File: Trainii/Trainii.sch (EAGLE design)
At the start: 30 parts, among them J1 APDS-9960, J2 Left Motor Encoder, J3 Right Motor Encoder, J4 Line Sensor 1, J5 Line Sensor 2, J6 Ultrasonic, J7 Left Motor Output, J8 Right Motor Output, J9 Lift Motor Output, U1 TPS61222DCKR, U2 BSS138

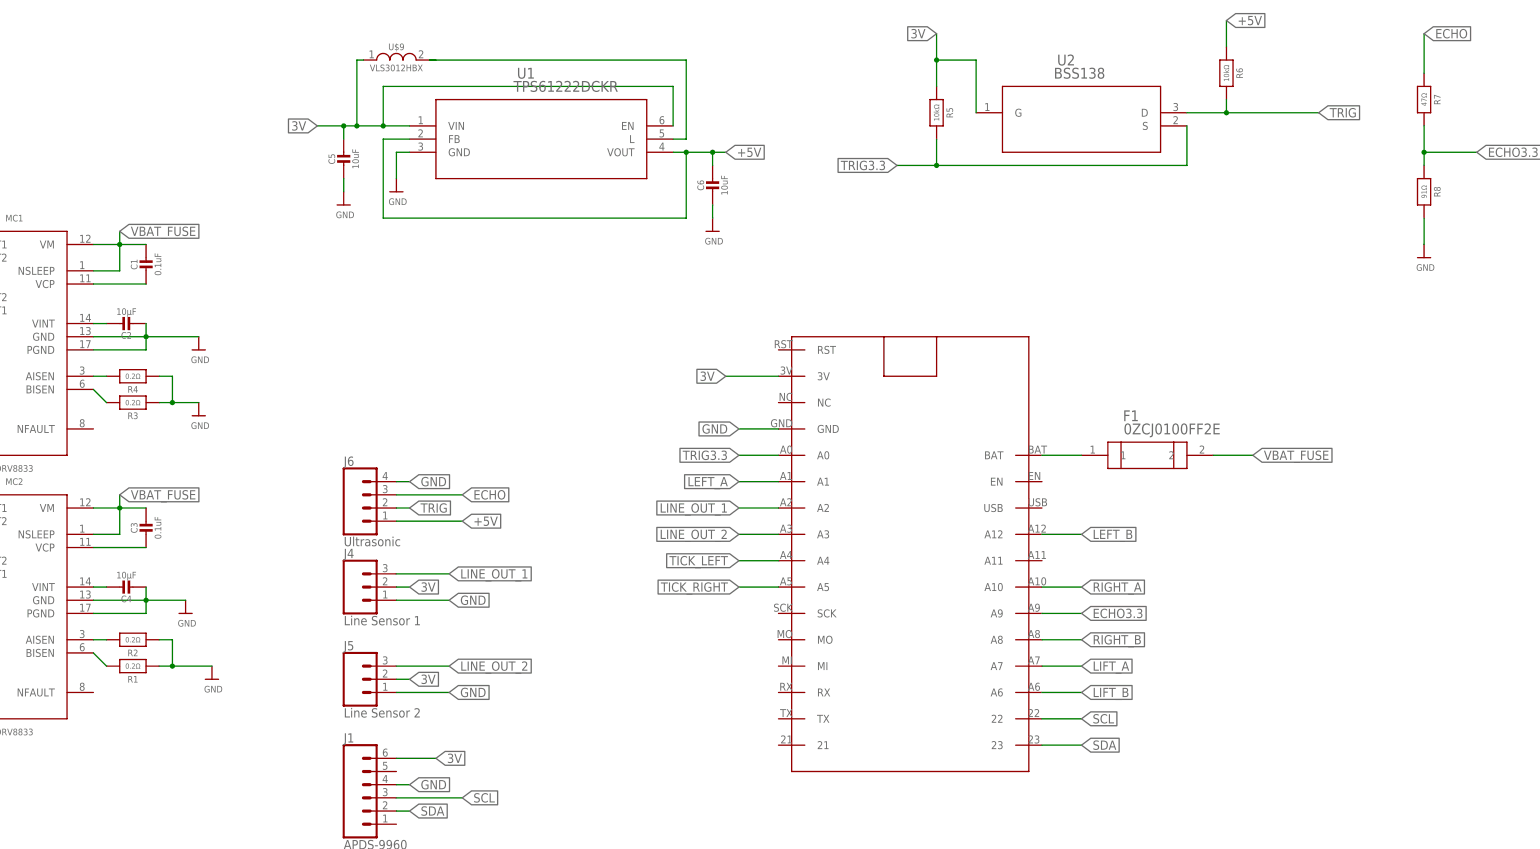
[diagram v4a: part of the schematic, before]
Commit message: Continued library update and finished schematic driver correction
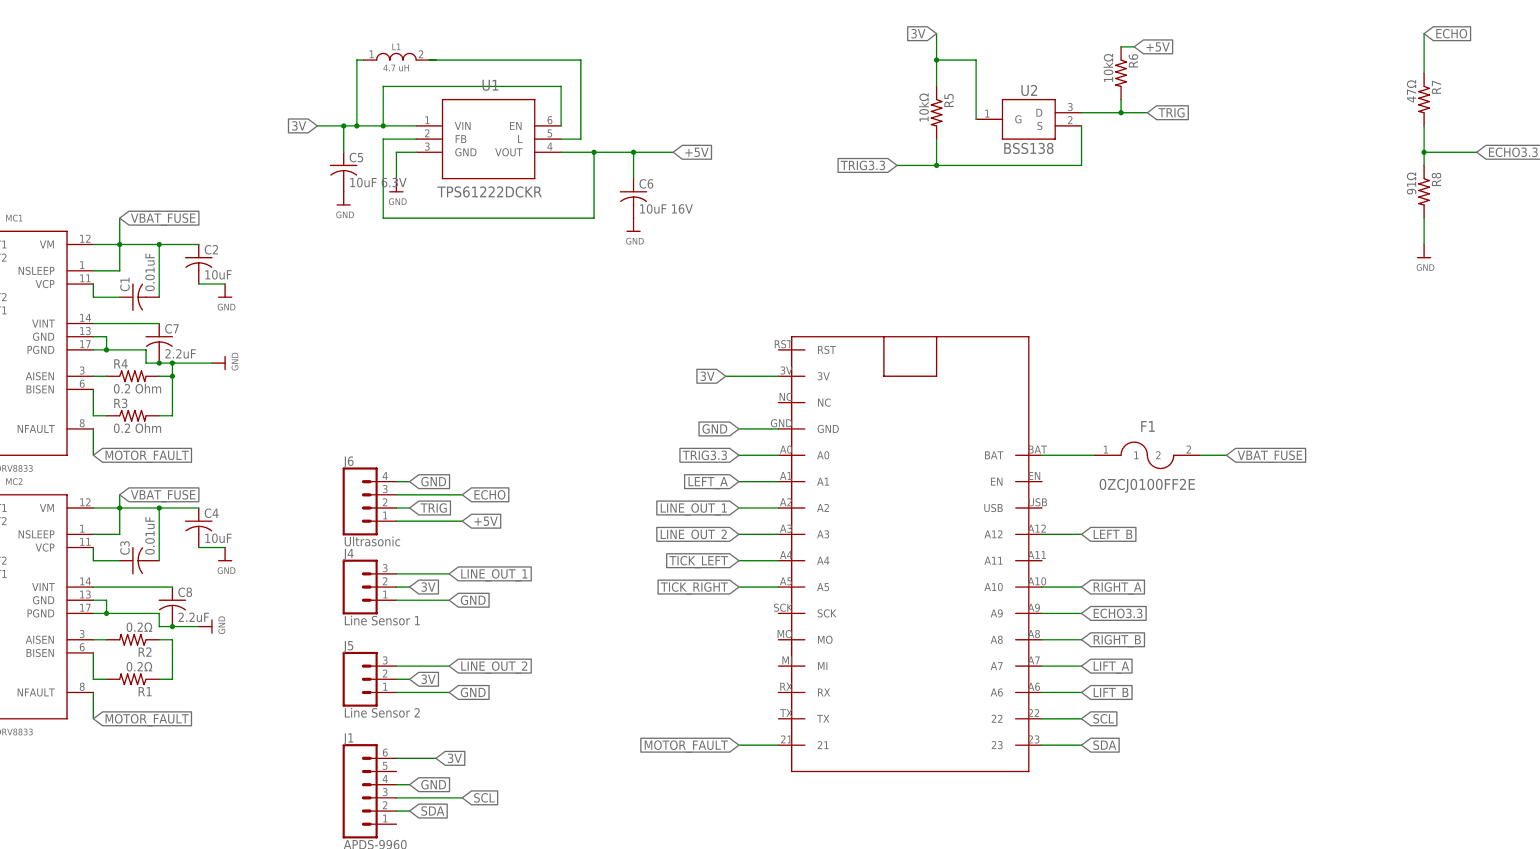
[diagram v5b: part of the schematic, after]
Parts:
- added C7, C8: 2.2uF, rcl:C-USC0805
- C1, C3: value 0.1uF -> 0.01uF; device microbuilder:CAP_CERAMIC0805-NOOUTLINE -> rcl:C-USC0805
- C2, C4: value 10µF -> 10uF; device microbuilder:CAP_CERAMIC0805-NOOUTLINE -> rcl:C-USC0805
- C5: value 10uF -> 10uF 6.3V; device microbuilder:CAP_CERAMIC0805-NOOUTLINE -> rcl:C-USC0805
- C6: value 10uF -> 10uF 16V; device microbuilder:CAP_CERAMIC0805-NOOUTLINE -> rcl:C-USC0805
- L1: value VLS3012HBX -> 4.7 uH
- R1, R2, R5, R6: device microbuilder:RESISTOR_1206 -> rcl:R-US_R0805
- R3, R4: value 0.2Ω -> 0.2 Ohm; device microbuilder:RESISTOR_1206 -> rcl:R-US_R0805
- R7, R8: device microbuilder:RESISTOR_1206 -> rcl:R-US_M0805
- renumbered U$9 to L1
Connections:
- removed net N$3: C3.2, MC2.VCP
- new net MOTOR_FAULT: MC1.NFAULT, MC2.NFAULT, U$6.21
- new net N$11: C3.1, MC2.VCP
- new net N$2: R1.1, R2.1
- net GND: now also C7.2, C8.2, R3.2, R4.2; no longer R1.1, R2.1, R3.1, R4.1
- net N$10: now also R4.1; no longer R4.2
- net N$5: now also C8.1; no longer C4.1
- net N$7: now also C1.1; no longer C1.2
- net N$8: now also C7.1; no longer C2.1
- net N$9: now also R3.1; no longer R3.2
- net VBAT_FUSE: now also C1.2, C2.1, C3.2, C4.1; no longer C1.1, C3.1, F1.2
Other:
- moved on the sheet: C1, C2, C3, C4, C5, C6, U1, U2

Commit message: Added new battery connector
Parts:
- added R10, R12: 91Ω, rcl:R-US_M0805
- added R11, R9: 47Ω, rcl:R-US_M0805
- added X1: JST-PH2, Trainii:JST-PH2
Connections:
- net ECHO renamed ECHO_5V
- net ECHO3.3 renamed ECHO_3V3
- net TRIG renamed TRIG_5V
- net TRIG3.3 renamed TRIG_3V3
- removed net 3V: C5.1, J1.6, J2.1, J3.1, J4.2, J5.2, L1.IN, R5.1, U$6.3V, U1.EN, U1.VIN, U2.G
- new net 3V3: C5.1, J1.6, J2.1, J3.1, L1.IN, R5.1, U$6.3V, U1.EN, U1.VIN, U2.G
- new net LINE_OUT_1_3V3: R10.1, R9.2
- new net LINE_OUT_1_5V: J4.3, R9.1
- new net LINE_OUT_2_3V3: R11.2, R12.1
- new net LINE_OUT_2_5V: J5.3, R11.1
- net +5V: now also J4.2, J5.2
- net GND: now also R10.2, R12.2, X1.1
- net LINE_OUT_1: no longer J4.3
- net LINE_OUT_2: no longer J5.3
- net VBAT: now also X1.2

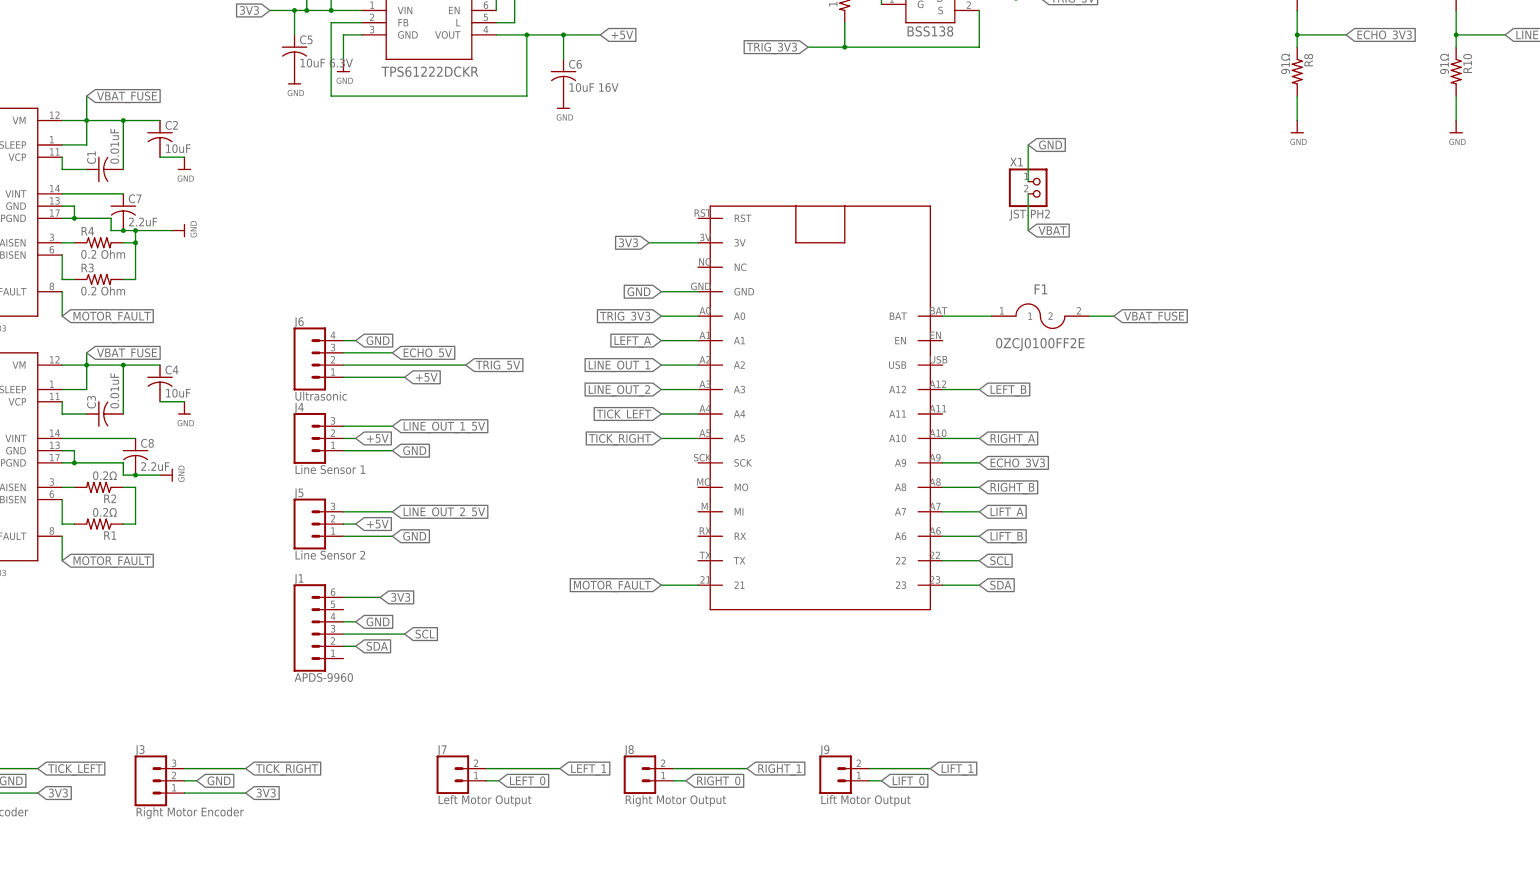
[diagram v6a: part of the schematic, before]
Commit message: edited schematic to include 3-position switch to select charging, running, or off
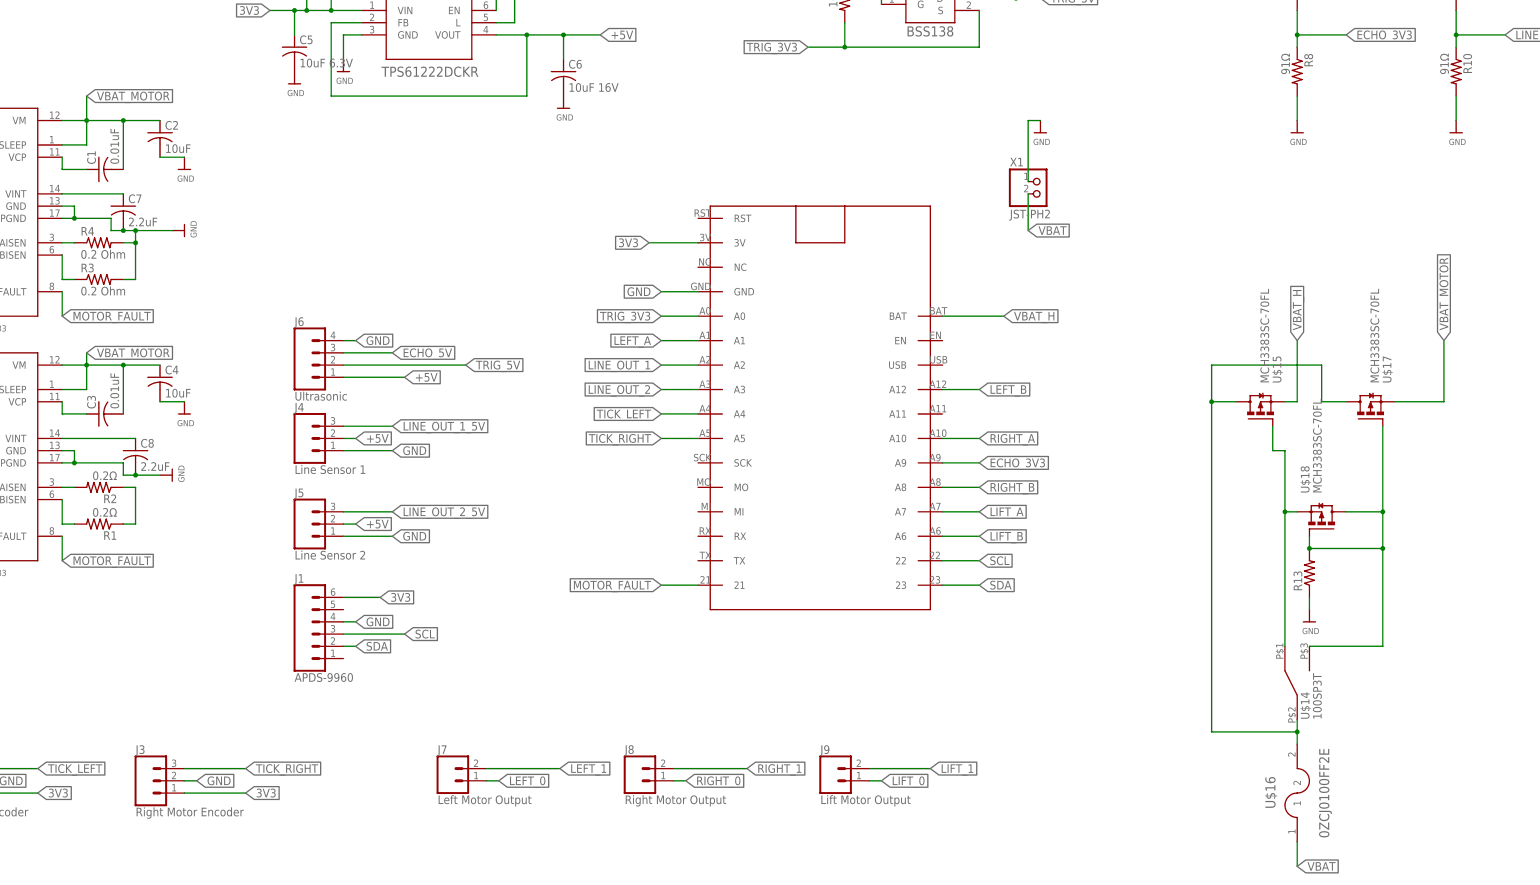
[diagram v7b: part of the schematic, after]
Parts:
- removed F1: 0ZCJ0100FF2E, Trainii:0ZCJ0100FF2E
- added R13: (no value), rcl:R-US_R0603
- added U$14: 100SP3T, Trainii:100SP3T
- added U$15, U$17, U$18: MCH3383SC-70FL, Trainii:MCH3383SC-70FL
- added U$16: 0ZCJ0100FF2E, Trainii:0ZCJ0100FF2E
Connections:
- removed net VBAT_FUSE: C1.2, C2.1, C3.2, C4.1, MC1.NSLEEP, MC1.VM, MC2.NSLEEP, MC2.VM
- new net N$13: R13.2, U$14.B, U$17.G, U$18.D, U$18.G
- new net N$3: U$14.A, U$15.G, U$18.S
- new net VBAT_H: U$15.S, U$6.BAT
- new net VBAT_MOTOR: C1.2, C2.1, C3.2, C4.1, MC1.NSLEEP, MC1.VM, MC2.NSLEEP, MC2.VM, U$17.S
- net GND: now also R13.1
- net VBAT: now also U$14.COMMON, U$15.D, U$16.1, U$16.2, U$17.D; no longer F1.1, U$6.BAT

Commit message: Updated Libraries, corrected component placement
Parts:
- removed U$14: 100SP3T, Trainii:100SP3T
- removed U$15, U$17, U$18: MCH3383SC-70FL, Trainii:MCH3383SC-70FL
- removed U$16: 0ZCJ0100FF2E, Trainii:0ZCJ0100FF2E
- added F1: 0ZCJ0100FF2E, Trainii:0ZCJ0100FF2E
- added S1: 100SP3T, Trainii:100SP3T
- added T1, T2, T3: MCH3383SC-70FL, Trainii:MCH3383SC-70FL
- L1: value 4.7 uH -> 4.7uH
- R13: value (none) -> 10kΩ
- R3, R4: value 0.2 Ohm -> 0.2Ω
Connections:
- removed net VBAT_H: U$15.S, U$6.BAT
- new net VBAT_HUZZAH: T2.S, U$6.BAT
- new net VBAT_MOTOR_FUSE: C1.2, C2.1, C3.2, C4.1, F1.2, MC1.NSLEEP, MC1.VM, MC2.NSLEEP, MC2.VM
- net N$13: now also S1.B, T1.D, T1.G, T3.G; no longer U$14.B, U$17.G, U$18.D, U$18.G
- net N$3: now also S1.A, T1.S, T2.G; no longer U$14.A, U$15.G, U$18.S
- net VBAT: now also S1.COMMON, T2.D, T3.D; no longer U$14.COMMON, U$15.D, U$16.1, U$16.2, U$17.D
- net VBAT_MOTOR: now also F1.1, T3.S; no longer C1.2, C2.1, C3.2, C4.1, MC1.NSLEEP, MC1.VM, MC2.NSLEEP, MC2.VM, U$17.S
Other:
- moved on the sheet: R13
